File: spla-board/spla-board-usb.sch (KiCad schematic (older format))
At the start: 24 parts, among them J1 USB_B_Micro, U2 FT2232H, U3 93LC66B, X1 FT5HNBPK12.0-T1

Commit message: schematic/pcb: Update for new KiCad version; no meaningfuly changes.
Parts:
- U2: symbol Interface_USB:FT2232H -> Interface_USB:FT2232HL
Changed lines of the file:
@@
 	3500 4450 3750 4450
 $Comp
-L Interface_USB:FT2232H U2
+L Interface_USB:FT2232HL U2
 U 1 1 5E5299CA
 P 9950 5650

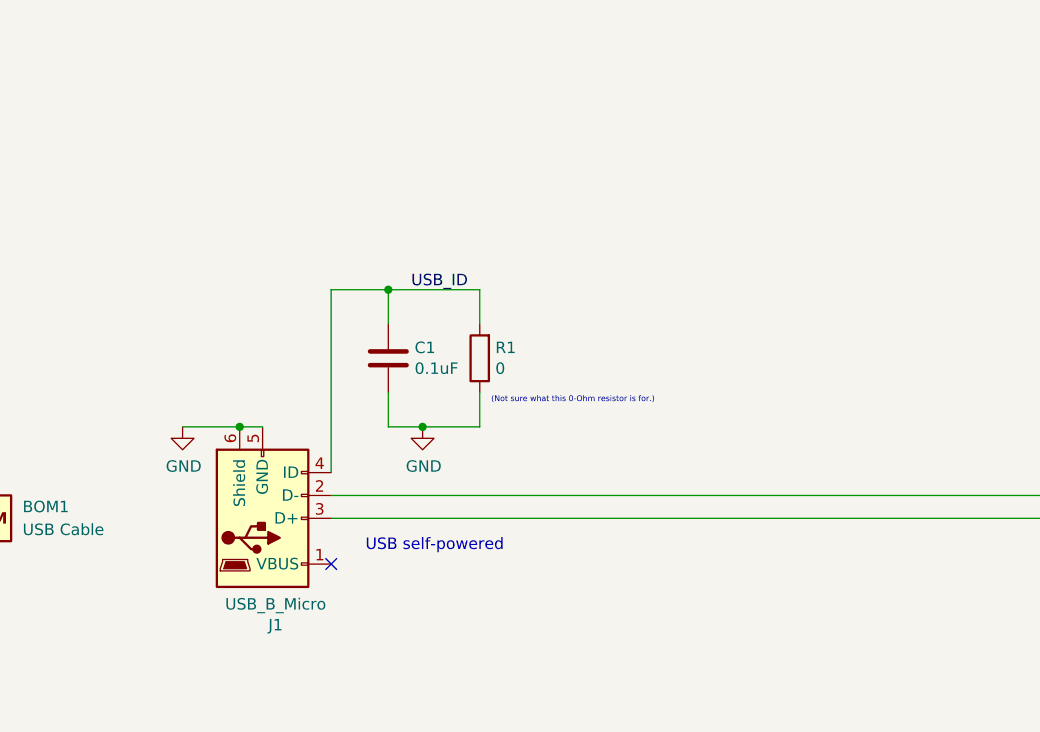
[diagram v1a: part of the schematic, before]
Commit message: schematic/pcb: Disconnect USB shield from ground.
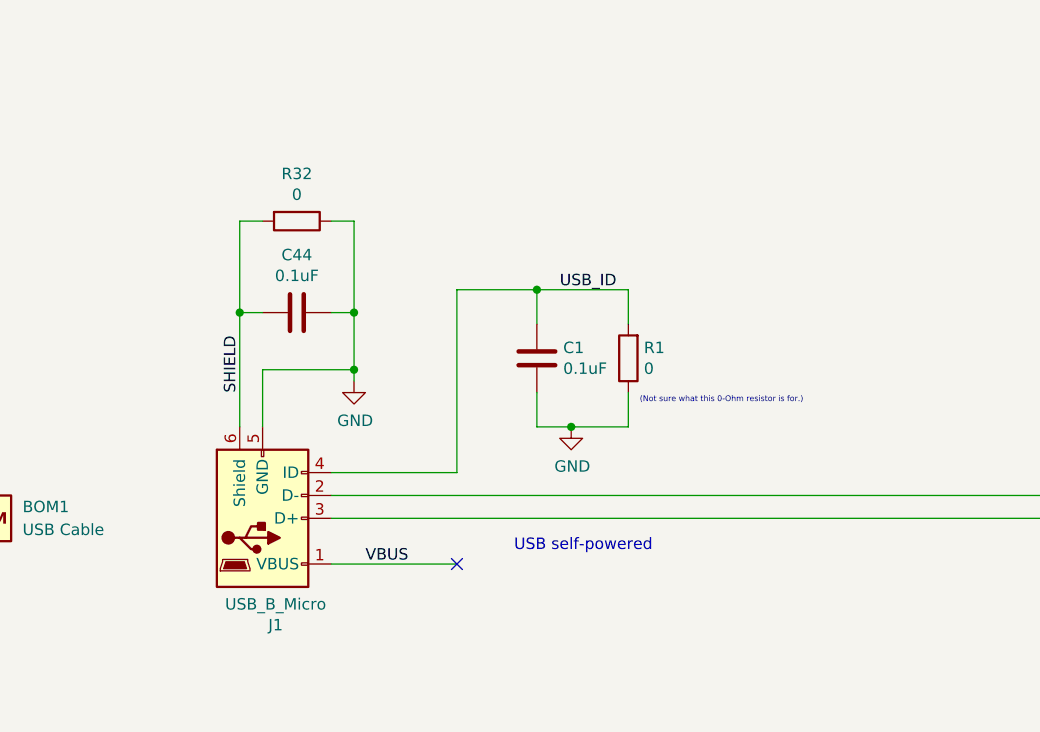
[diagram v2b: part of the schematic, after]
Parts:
- added C44: 0.1uF, Capacitor_SMD:C_0603_1608Metric, symbol Device:C
- added R32: 0, Resistor_SMD:R_0603_1608Metric, symbol Device:R
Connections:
- net GND: now also C44.1, R32.1; no longer J1.6 (Shield)
- net VBUS: now reaches J1.1 (VBUS)
- new net SHIELD: C44.2, J1.6 (Shield), R32.2
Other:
- moved on the sheet: C1, R1

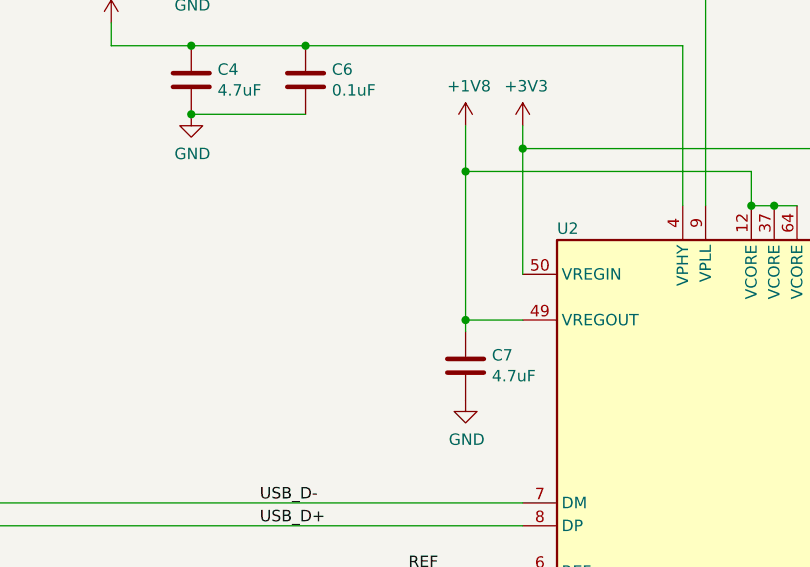
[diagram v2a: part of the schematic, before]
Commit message: schematic/pcb: Add test point for 1.8V FTDI regulator.
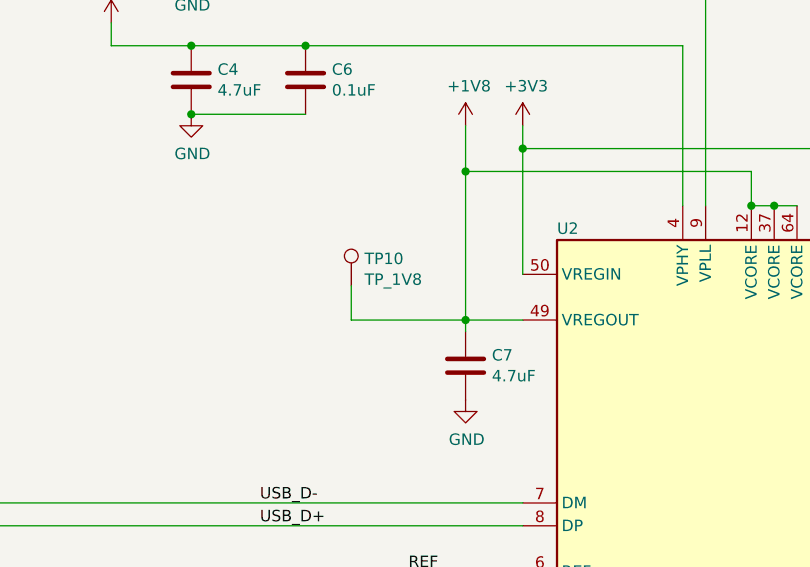
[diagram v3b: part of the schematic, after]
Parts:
- added TP10: TP_1V8, TestPoint:TestPoint_Pad_D2.0mm, symbol Connector:TestPoint
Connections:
- net +1V8: now also TP10.1
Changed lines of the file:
@@
 	10150 7850 10050 7850
 NoConn ~ 8750 7250
-Wire Wire Line
-	7550 7900 8100 7900
-Wire Wire Line
-	8100 7900 8100 6850
-Wire Wire Line
-	8100 6850 8750 6850
 $Comp
 L power:GND #PWR0104
@@
 Wire Wire Line
 	3100 4750 8750 4750
-Text GLabel 8300 8300 2    50   Output ~ 0
-CLK_12MHZ
-Wire Wire Line
-	8100 7900 8100 8300
-Wire Wire Line
-	8100 8300 8300 8300
-Connection ~ 8100 7900
 Wire Wire Line
 	6350 7450 6350 7600
@@
 VBUS
 NoConn ~ 3650 5050
+$Comp
+L Connector:TestPoint TP10
+U 1 1 5F33FE5B
+P 8000 3800
+F 0 "TP10" H 8058 3918 50  0000 L CNN
+F 1 "TP_1V8" H 8058 3827 50  0000 L CNN
+F 2 "TestPoint:TestPoint_Pad_D2.0mm" H 8200 3800 50  0001 C CNN
+F 3 "~" H 8200 3800 50  0001 C CNN
+	1    8000 3800
+	1    0    0    -1
+$EndComp
+Wire Wire Line
+	8500 3950 8000 3950
+Wire Wire Line
+	8000 3950 8000 3800
+Text GLabel 8300 8300 2    50   Output ~ 0
+CLK_12MHZ
+Wire Wire Line
+	8100 8300 8300 8300
+Connection ~ 8100 7900
+Wire Wire Line
+	8100 7900 8100 8300
+Wire Wire Line
+	8100 6850 8750 6850
+Wire Wire Line
+	8100 7900 8100 6850
+Wire Wire Line
+	7550 7900 8100 7900
 $EndSCHEMATC

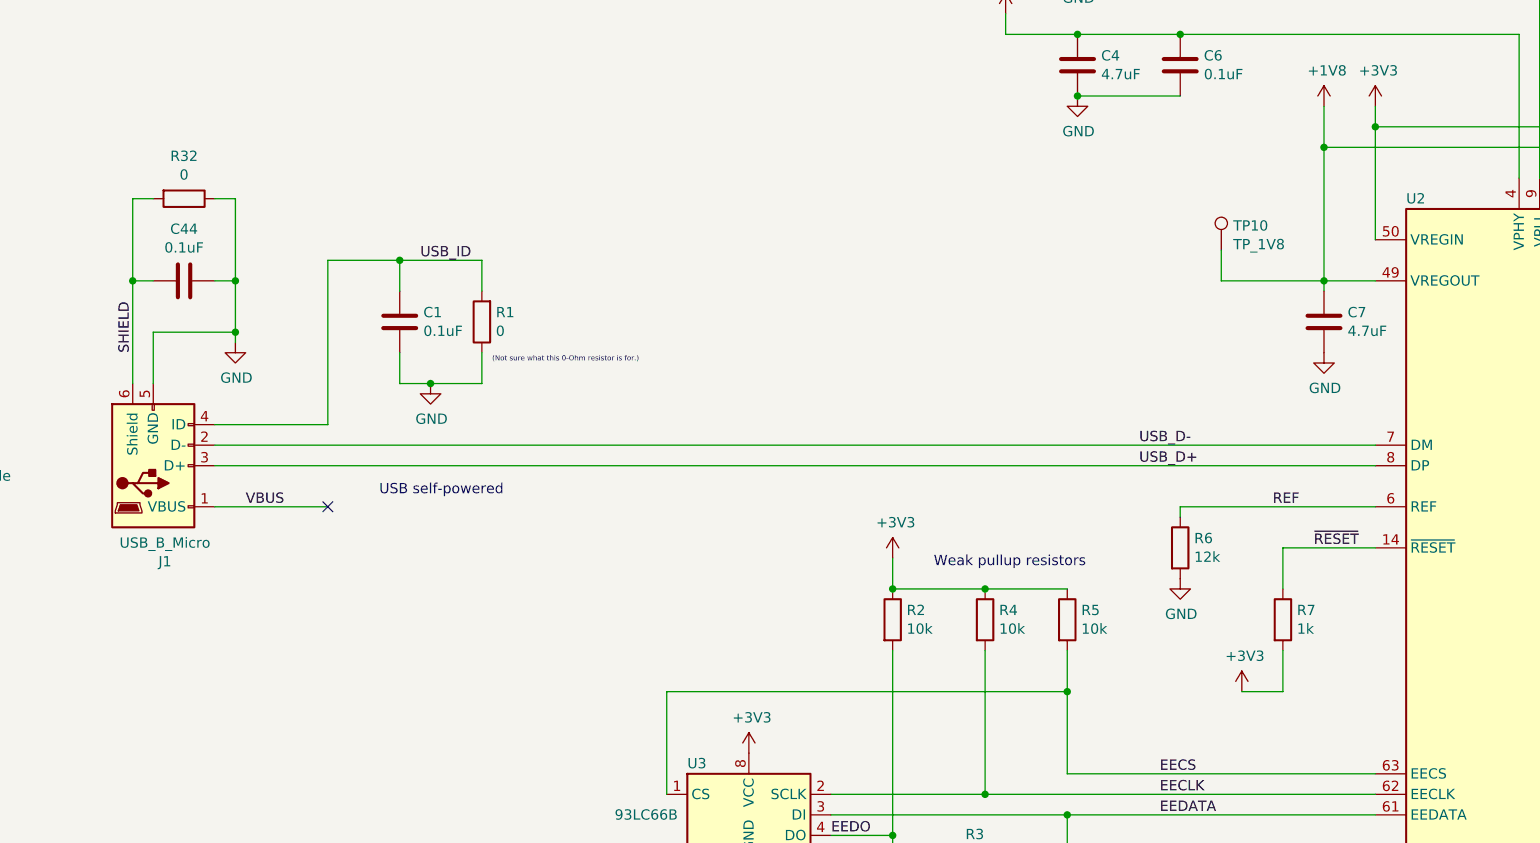
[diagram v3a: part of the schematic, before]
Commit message: schematic/pcb: Add reset "switch" via shortable resistor pads
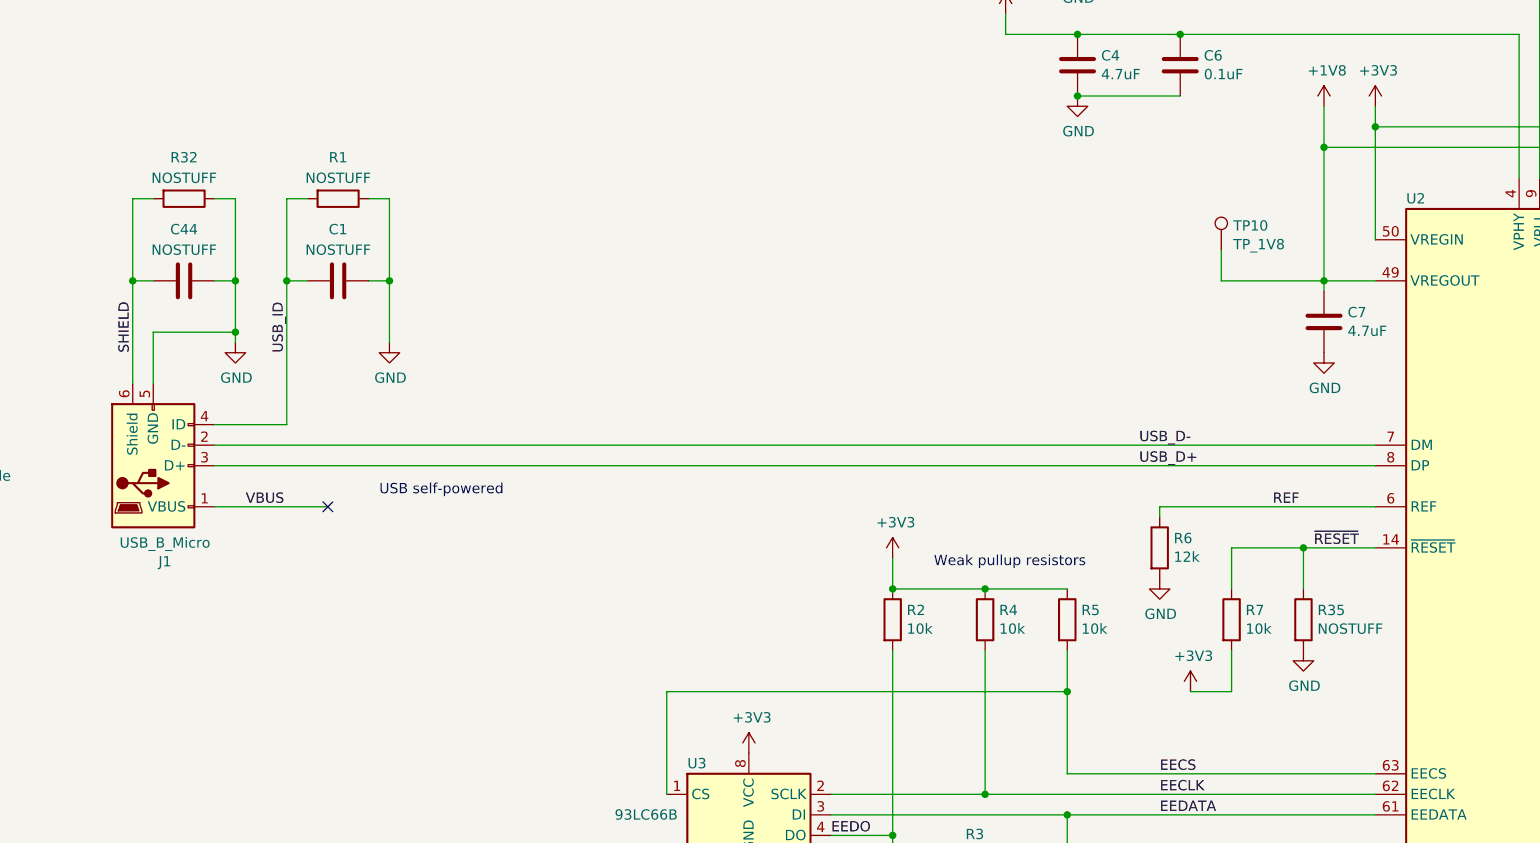
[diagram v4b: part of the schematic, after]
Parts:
- added R35: NOSTUFF, Resistor_SMD:R_0603_1608Metric, symbol Device:R
- C1, C44: value 0.1uF -> NOSTUFF; Digikey 490-16477-1-ND -> N/A; Manufacturer Murata Electronics -> N/A; Manufacturer Id GCJ188R71E104KA12D -> N/A
- R1: value 0 -> NOSTUFF; Digikey 2019-RK73Z1JTTDCT-ND -> N/A; Manufacturer KOA Speer Electronics Inc. -> N/A; Manufacturer Id RK73Z1JTTD -> N/A
- R32: value 0 -> NOSTUFF; Digikey 2019-RK73Z1JTTDCT-ND -> N/A; Manufacturer Stackpole Electronics Inc -> N/A; Manufacturer Id RK73Z1JTTD -> N/A
- R7: value 1k -> 10k; Digikey RMCF0603JT1K00CT-ND -> RMCF0603JT10K0CT-ND; Manufacturer Id RMCF0603JT1K00 -> RMCF0603JT10K0
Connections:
- net GND: now also R35.2
- net ~RESET: now also R35.1
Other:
- note removed: "(Not sure what this 0-Ohm resistor is for.)"
- moved on the sheet: C1, R1, R6, R7
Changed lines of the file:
@@
 L Device:R R1
 U 1 1 5E4AB80E
-P 4400 4150
-F 0 "R1" H 4332 4104 50  0000 R CNN
-F 1 "0" H 4332 4195 50  0000 R CNN
-F 2 "Resistor_SMD:R_0603_1608Metric" V 4440 4140 50  0001 C CNN
-F 3 "~" H 4400 4150 50  0001 C CNN
-F 4 "2019-RK73Z1JTTDCT-ND" H 4400 4150 50  0001 C CNN "Digikey"
-F 5 "KOA Speer Electronics Inc." H 4400 4150 50  0001 C CNN "Manufacturer"
-F 6 "RK73Z1JTTD" H 4400 4150 50  0001 C CNN "Manufacturer Id"
-	1    4400 4150
-	-1   0    0    1
+P 3700 3550
+F 0 "R1" V 3500 3550 50  0000 C CNN
+F 1 "NOSTUFF" V 3600 3550 50  0000 C CNN
+F 2 "Resistor_SMD:R_0603_1608Metric" V 3740 3540 50  0001 C CNN
+F 3 "~" H 3700 3550 50  0001 C CNN
+F 4 "N/A" H 3700 3550 50  0001 C CNN "Digikey"
+F 5 "N/A" H 3700 3550 50  0001 C CNN "Manufacturer"
+F 6 "N/A" H 3700 3550 50  0001 C CNN "Manufacturer Id"
+	1    3700 3550
+	0    1    1    0
 $EndComp
 $Comp
@@
 L Device:C C1
 U 1 1 5E4ACE23
-P 4000 4150
-F 0 "C1" H 3885 4104 50  0000 R CNN
-F 1 "0.1uF" H 3885 4195 50  0000 R CNN
-F 2 "Capacitor_SMD:C_0603_1608Metric" H 4038 4000 50  0001 C CNN
-F 3 "~" H 4000 4150 50  0001 C CNN
-F 4 "490-16477-1-ND" H 4000 4150 50  0001 C CNN "Digikey"
-F 5 "Murata Electronics" H 4000 4150 50  0001 C CNN "Manufacturer"
-F 6 "GCJ188R71E104KA12D" H 4000 4150 50  0001 C CNN "Manufacturer Id"
-	1    4000 4150
-	-1   0    0    1
-$EndComp
-Wire Wire Line
-	4400 3850 4400 4000
-Wire Wire Line
-	4000 4000 4000 3850
-Connection ~ 4000 3850
-Wire Wire Line
-	4000 3850 4400 3850
-Wire Wire Line
-	4000 4300 4000 4450
-Wire Wire Line
-	4400 4300 4400 4450
+P 3700 3950
+F 0 "C1" V 3450 3950 50  0000 C CNN
+F 1 "NOSTUFF" V 3550 3950 50  0000 C CNN
+F 2 "Capacitor_SMD:C_0603_1608Metric" H 3738 3800 50  0001 C CNN
+F 3 "~" H 3700 3950 50  0001 C CNN
+F 4 "N/A" H 3700 3950 50  0001 C CNN "Digikey"
+F 5 "N/A" H 3700 3950 50  0001 C CNN "Manufacturer"
+F 6 "N/A" H 3700 3950 50  0001 C CNN "Manufacturer Id"
+	1    3700 3950
+	0    1    1    0
+$EndComp
+Wire Wire Line
+	3450 3550 3550 3550
+Wire Wire Line
+	3850 3550 3950 3550
 $Comp
 L power:GND #PWR0102
 U 1 1 5E4C66E6
-P 4150 4450
-F 0 "#PWR0102" H 4150 4200 50  0001 C CNN
-F 1 "GND" H 4155 4277 50  0000 C CNN
-F 2 "" H 4150 4450 50  0001 C CNN
-F 3 "" H 4150 4450 50  0001 C CNN
-	1    4150 4450
-	1    0    0    -1
-$EndComp
-Wire Wire Line
-	4000 4450 4150 4450
-Connection ~ 4150 4450
-Wire Wire Line
-	4150 4450 4400 4450
+P 3950 4250
+F 0 "#PWR0102" H 3950 4000 50  0001 C CNN
+F 1 "GND" H 3955 4077 50  0000 C CNN
+F 2 "" H 3950 4250 50  0001 C CNN
+F 3 "" H 3950 4250 50  0001 C CNN
+	1    3950 4250
+	1    0    0    -1
+$EndComp
 $Comp
 L Interface_USB:FT2232HL U2
@@
 L power:GND #PWR0108
 U 1 1 5E616CF7
-P 7800 5400
-F 0 "#PWR0108" H 7800 5150 50  0001 C CNN
-F 1 "GND" H 7805 5227 50  0000 C CNN
-F 2 "" H 7800 5400 50  0001 C CNN
-F 3 "" H 7800 5400 50  0001 C CNN
-	1    7800 5400
-	1    0    0    -1
-$EndComp
-Wire Wire Line
-	7800 5050 7800 5100
-Wire Wire Line
-	8300 5950 8300 5750
-Wire Wire Line
-	8300 5450 8300 5250
-Wire Wire Line
-	8300 5950 8100 5950
+P 7700 5400
+F 0 "#PWR0108" H 7700 5150 50  0001 C CNN
+F 1 "GND" H 7705 5227 50  0000 C CNN
+F 2 "" H 7700 5400 50  0001 C CNN
+F 3 "" H 7700 5400 50  0001 C CNN
+	1    7700 5400
+	1    0    0    -1
+$EndComp
+Wire Wire Line
+	7700 5050 7700 5100
+Wire Wire Line
+	8050 5950 8050 5750
+Wire Wire Line
+	8050 5450 8050 5250
+Wire Wire Line
+	8050 5950 7850 5950
 Wire Wire Line
 	9750 3450 9750 3300
@@
 L power:+3V3 #PWR0111
 U 1 1 5E64AC08
-P 8100 5950
-F 0 "#PWR0111" H 8100 5800 50  0001 C CNN
-F 1 "+3V3" H 8115 6123 50  0000 C CNN
-F 2 "" H 8100 5950 50  0001 C CNN
-F 3 "" H 8100 5950 50  0001 C CNN
-	1    8100 5950
+P 7850 5950
+F 0 "#PWR0111" H 7850 5800 50  0001 C CNN
+F 1 "+3V3" H 7865 6123 50  0000 C CNN
+F 2 "" H 7850 5950 50  0001 C CNN
+F 3 "" H 7850 5950 50  0001 C CNN
+	1    7850 5950
 	1    0    0    -1
 $EndComp
@@
 Wire Wire Line
 	8750 3200 8750 3100
-Text Notes 4450 4350 0    25   ~ 0
-(Not sure what this 0-Ohm resistor is for.)
 Wire Wire Line
 	9450 3450 9450 2750
@@
 EECLK
 Wire Wire Line
-	7800 5050 8750 5050
+	7700 5050 8750 5050
 Text Label 8250 5050 0    50   ~ 0
 REF
 Wire Wire Line
-	8300 5250 8750 5250
+	8050 5250 8400 5250
 Text Label 8450 5250 0    50   ~ 0
 ~RESET
@@
 Text Label 7600 4850 0    50   ~ 0
 USB_D+
-Text Label 4100 3850 0    50   ~ 0
+Text Label 3450 4300 1    50   ~ 0
 USB_ID
 Text Label 6100 6650 0    50   ~ 0
@@
 	3200 3950 3200 4200
 Wire Wire Line
-	3100 4650 3650 4650
-Wire Wire Line
-	3650 4650 3650 3850
-Wire Wire Line
-	3650 3850 4000 3850
+	3100 4650 3450 4650
+Wire Wire Line
+	3450 4650 3450 3950
 Wire Wire Line
 	2700 4450 2700 3950
@@
 L Device:R R7
 U 1 1 5E619C52
-P 8300 5600
-F 0 "R7" H 8368 5646 50  0000 L CNN
-F 1 "1k" H 8368 5555 50  0000 L CNN
-F 2 "Resistor_SMD:R_0603_1608Metric" V 8340 5590 50  0001 C CNN
-F 3 "~" H 8300 5600 50  0001 C CNN
-F 4 "RMCF0603JT1K00CT-ND" H 8300 5600 50  0001 C CNN "Digikey"
-F 5 "Stackpole Electronics Inc" H 8300 5600 50  0001 C CNN "Manufacturer"
-F 6 "RMCF0603JT1K00" H 8300 5600 50  0001 C CNN "Manufacturer Id"
-	1    8300 5600
+P 8050 5600
+F 0 "R7" H 8118 5646 50  0000 L CNN
+F 1 "10k" H 8118 5555 50  0000 L CNN
+F 2 "Resistor_SMD:R_0603_1608Metric" V 8090 5590 50  0001 C CNN
+F 3 "~" H 8050 5600 50  0001 C CNN
+F 4 "RMCF0603JT10K0CT-ND" H 8050 5600 50  0001 C CNN "Digikey"
+F 5 "Stackpole Electronics Inc" H 8050 5600 50  0001 C CNN "Manufacturer"
+F 6 "RMCF0603JT10K0" H 8050 5600 50  0001 C CNN "Manufacturer Id"
+	1    8050 5600
 	1    0    0    -1
 $EndComp
@@
 L Device:R R6
 U 1 1 5E60E8AF
-P 7800 5250
-F 0 "R6" H 7868 5296 50  0000 L CNN
-F 1 "12k" H 7868 5205 50  0000 L CNN
-F 2 "Resistor_SMD:R_0603_1608Metric" V 7840 5240 50  0001 C CNN
-F 3 "~" H 7800 5250 50  0001 C CNN
-F 4 "RMCF0603JT12K0CT-ND" H 7800 5250 50  0001 C CNN "Digikey"
-F 5 "Stackpole Electronics Inc" H 7800 5250 50  0001 C CNN "Manufacturer"
-F 6 "RMCF0603JT12K0" H 7800 5250 50  0001 C CNN "Manufacturer Id"
-	1    7800 5250
+P 7700 5250
+F 0 "R6" H 7768 5296 50  0000 L CNN
+F 1 "12k" H 7768 5205 50  0000 L CNN
+F 2 "Resistor_SMD:R_0603_1608Metric" V 7740 5240 50  0001 C CNN
+F 3 "~" H 7700 5250 50  0001 C CNN
+F 4 "RMCF0603JT12K0CT-ND" H 7700 5250 50  0001 C CNN "Digikey"
+F 5 "Stackpole Electronics Inc" H 7700 5250 50  0001 C CNN "Manufacturer"
+F 6 "RMCF0603JT12K0" H 7700 5250 50  0001 C CNN "Manufacturer Id"
+	1    7700 5250
 	1    0    0    -1
 $EndComp
@@
 U 1 1 5F34ED5D
 P 2950 3550
-F 0 "R32" V 2743 3550 50  0000 C CNN
-F 1 "0" V 2834 3550 50  0000 C CNN
+F 0 "R32" V 2750 3550 50  0000 C CNN
+F 1 "NOSTUFF" V 2850 3550 50  0000 C CNN
 F 2 "Resistor_SMD:R_0603_1608Metric" H 2950 3550 50  0001 C CNN
 F 3 "~" H 2950 3550 50  0001 C CNN
-F 4 "2019-RK73Z1JTTDCT-ND" H 2950 3550 50  0001 C CNN "Digikey"
-F 5 "Stackpole Electronics Inc" H 2950 3550 50  0001 C CNN "Manufacturer"
-F 6 "RK73Z1JTTD" H 2950 3550 50  0001 C CNN "Manufacturer Id"
+F 4 "N/A" H 2950 3550 50  0001 C CNN "Digikey"
+F 5 "N/A" H 2950 3550 50  0001 C CNN "Manufacturer"
+F 6 "N/A" H 2950 3550 50  0001 C CNN "Manufacturer Id"
 	1    2950 3550
 	0    1    1    0
@@
 U 1 1 5F34D947
 P 2950 3950
-F 0 "C44" V 2698 3950 50  0000 C CNN
-F 1 "0.1uF" V 2789 3950 50  0000 C CNN
+F 0 "C44" V 2700 3950 50  0000 C CNN
+F 1 "NOSTUFF" V 2800 3950 50  0000 C CNN
 F 2 "Capacitor_SMD:C_0603_1608Metric" H 2950 3950 50  0001 C CNN
 F 3 "~" H 2950 3950 50  0001 C CNN
-F 4 "490-16477-1-ND" V 2950 3950 50  0001 C CNN "Digikey"
-F 5 "Murata Electronics" H 2950 3950 50  0001 C CNN "Manufacturer"
-F 6 "GCJ188R71E104KA12D" H 2950 3950 50  0001 C CNN "Manufacturer Id"
+F 4 "N/A" V 2950 3950 50  0001 C CNN "Digikey"
+F 5 "N/A" H 2950 3950 50  0001 C CNN "Manufacturer"
+F 6 "N/A" H 2950 3950 50  0001 C CNN "Manufacturer Id"
 	1    2950 3950
 	0    1    1    0
@@
 Wire Wire Line
 	7550 7900 8100 7900
+$Comp
+L Device:R R35
+U 1 1 5F34C3CC
+P 8400 5600
+F 0 "R35" H 8468 5646 50  0000 L CNN
+F 1 "NOSTUFF" H 8468 5555 50  0000 L CNN
+F 2 "Resistor_SMD:R_0603_1608Metric" V 8440 5590 50  0001 C CNN
+F 3 "~" H 8400 5600 50  0001 C CNN
+F 4 "RMCF0603JT1K00CT-ND" H 8400 5600 50  0001 C CNN "Digikey"
+F 5 "Stackpole Electronics Inc" H 8400 5600 50  0001 C CNN "Manufacturer"
+F 6 "RMCF0603JT1K00" H 8400 5600 50  0001 C CNN "Manufacturer Id"
+	1    8400 5600
+	1    0    0    -1
+$EndComp
+Wire Wire Line
+	8400 5250 8400 5450
+Connection ~ 8400 5250
+Wire Wire Line
+	8400 5250 8750 5250
+$Comp
+L power:GND #PWR0233
+U 1 1 5F35C8C6
+P 8400 5750
+F 0 "#PWR0233" H 8400 5500 50  0001 C CNN
+F 1 "GND" H 8405 5577 50  0000 C CNN
+F 2 "" H 8400 5750 50  0001 C CNN
+F 3 "" H 8400 5750 50  0001 C CNN
+	1    8400 5750
+	1    0    0    -1
+$EndComp
+Wire Wire Line
+	3550 3950 3450 3950
+Connection ~ 3450 3950
+Wire Wire Line
+	3450 3950 3450 3550
+Wire Wire Line
+	3950 3550 3950 3950
+Wire Wire Line
+	3850 3950 3950 3950
+Connection ~ 3950 3950
+Wire Wire Line
+	3950 3950 3950 4250
 $EndSCHEMATC
